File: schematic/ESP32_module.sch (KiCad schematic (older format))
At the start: 14 parts, among them J1 Conn_02x03_Odd_Even, J2 Conn_02x05_Odd_Even, J3 Conn_02x05_Odd_Even, U1 ESP32-WROOM-32

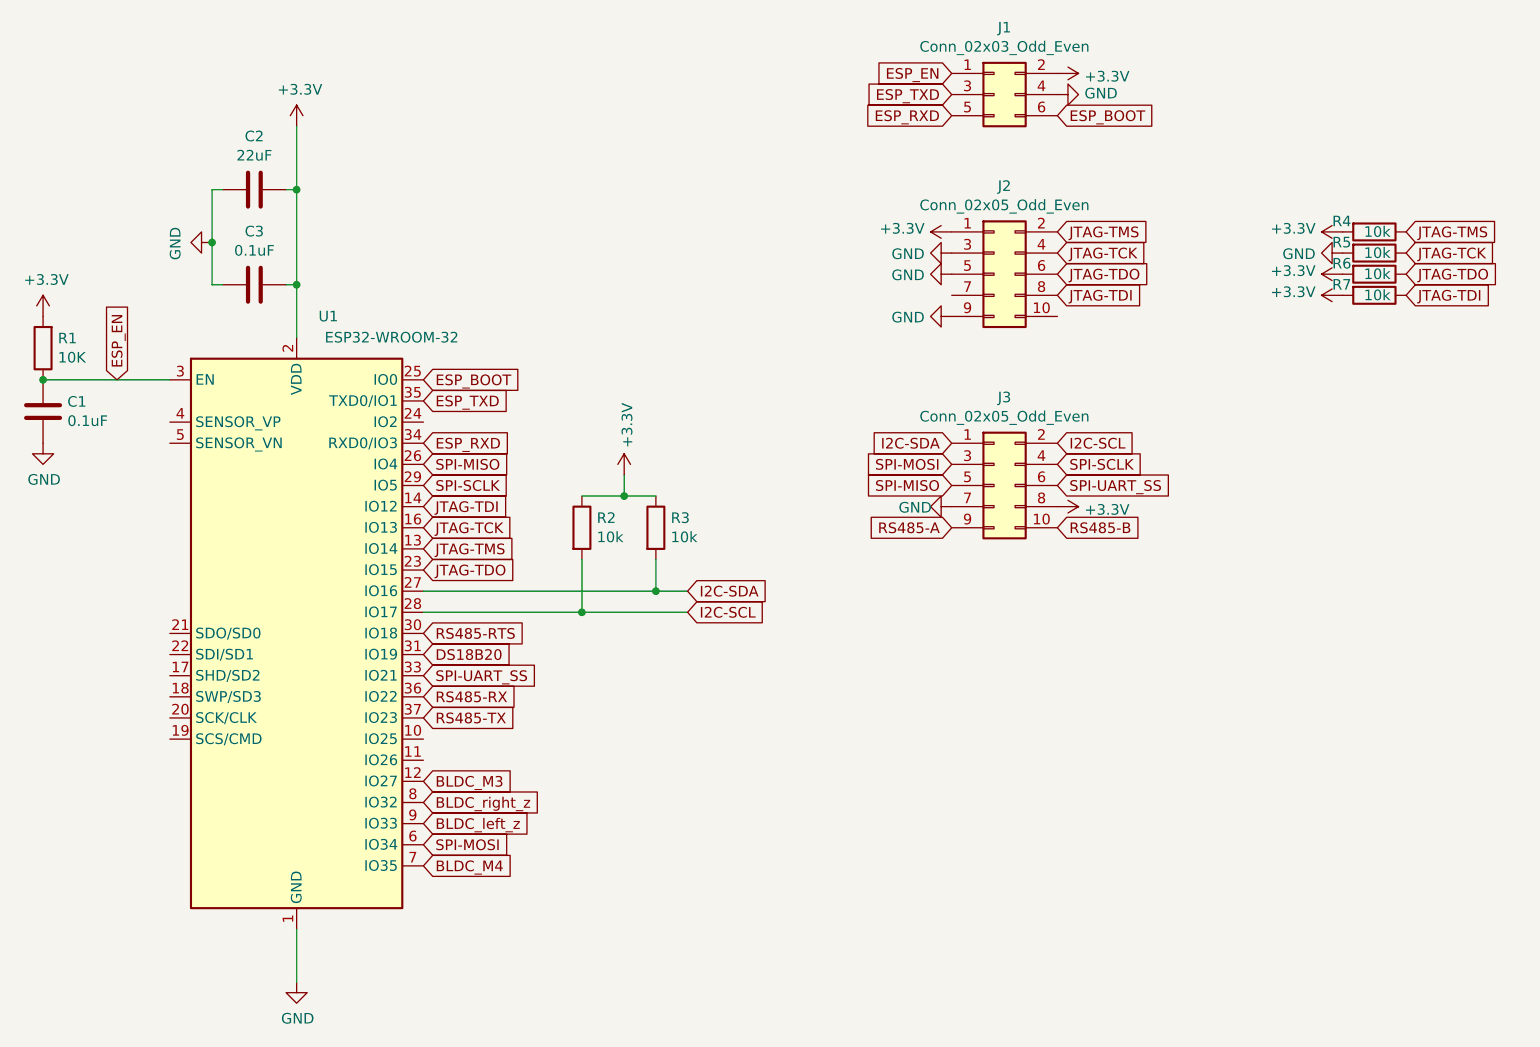
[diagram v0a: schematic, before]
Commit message: SPI SS multiplex concept
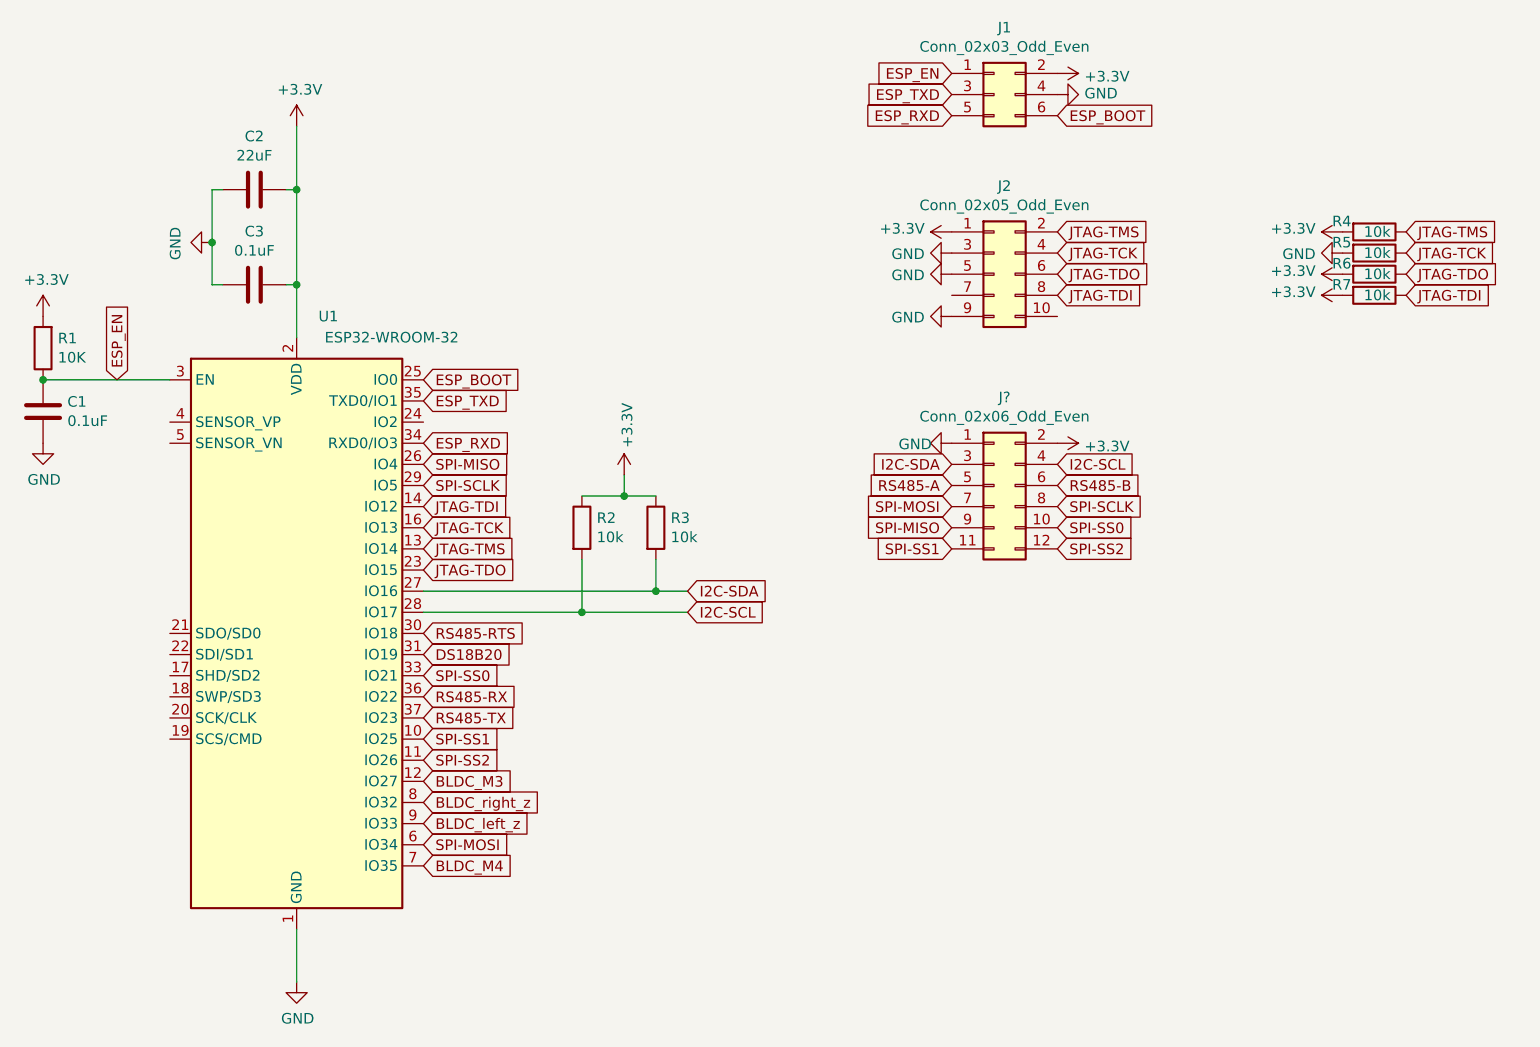
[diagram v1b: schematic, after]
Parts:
- removed J3: Conn_02x05_Odd_Even, Connector_IDC:IDC-Header_2x05_P2.54mm_Vertical, symbol Connector_Generic:Conn_02x05_Odd_Even
- added J?: Conn_02x06_Odd_Even, symbol Connector_Generic:Conn_02x06_Odd_Even
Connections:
- net +3V3: now also J?.2 (Pin_2)
- net GND: now also J?.1 (Pin_1)
- net I2C-SCL: now also J?.4 (Pin_4)
- net I2C-SDA: now also J?.3 (Pin_3)
- net RS485-A: now also J?.5 (Pin_5)
- net RS485-B: now also J?.6 (Pin_6)
- net SPI-MISO: now also J?.9 (Pin_9)
- net SPI-MOSI: now also J?.7 (Pin_7)
- net SPI-SCLK: now also J?.8 (Pin_8)
- net SPI-SS1: now reaches U1.10 (IO25)
- net SPI-SS1: now also J?.11 (Pin_11)
- net SPI-SS2: now reaches U1.11 (IO26)
- net SPI-SS2: now also J?.12 (Pin_12)
- net SPI-UART_SS renamed SPI-SS0
- net SPI-SS0: now also J?.10 (Pin_10)
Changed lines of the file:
@@
 SPI-SCLK
 Text GLabel 3150 4500 2    50   Input ~ 0
-SPI-UART_SS
+SPI-SS0
 Text GLabel 3150 4400 2    50   Input ~ 0
 DS18B20
@@
 	1    0    0    -1
 $EndComp
-$Comp
-L Connector_Generic:Conn_02x05_Odd_Even J?
-U 1 1 5EF14A1B
-P 5850 3600
-AR Path="/5EF14A1B" Ref="J?"  Part="1"
-AR Path="/5ED629AF/5EF14A1B" Ref="J3"  Part="1"
-F 0 "J3" H 5900 4017 50  0000 C CNN
-F 1 "Conn_02x05_Odd_Even" H 5900 3926 50  0000 C CNN
-F 2 "Connector_IDC:IDC-Header_2x05_P2.54mm_Vertical" H 5850 3600 50  0001 C CNN
-F 3 "~" H 5850 3600 50  0001 C CNN
-	1    5850 3600
-	1    0    0    -1
-$EndComp
-Text GLabel 5650 3400 0    50   Input ~ 0
+Text GLabel 5650 3500 0    50   Input ~ 0
 I2C-SDA
-Text GLabel 6150 3400 2    50   Input ~ 0
+Text GLabel 6150 3500 2    50   Input ~ 0
 I2C-SCL
 $Comp
 L power:GND #PWR?
 U 1 1 5EF14A23
-P 5650 3700
+P 5650 3400
 AR Path="/5EF14A23" Ref="#PWR?"  Part="1"
 AR Path="/5ED629AF/5EF14A23" Ref="#PWR011"  Part="1"
-F 0 "#PWR011" H 5650 3450 50  0001 C CNN
-F 1 "GND" V 5655 3527 50  0000 C CNN
-F 2 "" H 5650 3700 50  0001 C CNN
-F 3 "" H 5650 3700 50  0001 C CNN
-	1    5650 3700
+F 0 "#PWR011" H 5650 3150 50  0001 C CNN
+F 1 "GND" V 5655 3227 50  0000 C CNN
+F 2 "" H 5650 3400 50  0001 C CNN
+F 3 "" H 5650 3400 50  0001 C CNN
+	1    5650 3400
 	0    1    1    0
 $EndComp
@@
 L power:+3.3V #PWR?
 U 1 1 5EF14A29
-P 6150 3700
+P 6150 3400
 AR Path="/5EF14A29" Ref="#PWR?"  Part="1"
 AR Path="/5ED629AF/5EF14A29" Ref="#PWR014"  Part="1"
-F 0 "#PWR014" H 6150 3550 50  0001 C CNN
-F 1 "+3.3V" V 6165 3828 50  0000 L CNN
-F 2 "" H 6150 3700 50  0001 C CNN
-F 3 "" H 6150 3700 50  0001 C CNN
-	1    6150 3700
-	0    1    1    0
-$EndComp
+F 0 "#PWR014" H 6150 3250 50  0001 C CNN
+F 1 "+3.3V" V 6165 3528 50  0000 L CNN
+F 2 "" H 6150 3400 50  0001 C CNN
+F 3 "" H 6150 3400 50  0001 C CNN
+	1    6150 3400
+	0    1    1    0
+$EndComp
+Text GLabel 5650 3600 0    50   Input ~ 0
+RS485-A
+Text GLabel 6150 3600 2    50   Input ~ 0
+RS485-B
+Text GLabel 5650 3700 0    50   Input ~ 0
+SPI-MOSI
 Text GLabel 5650 3800 0    50   Input ~ 0
-RS485-A
+SPI-MISO
+Text GLabel 6150 3700 2    50   Input ~ 0
+SPI-SCLK
 Text GLabel 6150 3800 2    50   Input ~ 0
-RS485-B
-Text GLabel 5650 3500 0    50   Input ~ 0
-SPI-MOSI
-Text GLabel 5650 3600 0    50   Input ~ 0
-SPI-MISO
-Text GLabel 6150 3500 2    50   Input ~ 0
-SPI-SCLK
-Text GLabel 6150 3600 2    50   Input ~ 0
-SPI-UART_SS
+SPI-SS0
 $Comp
 L Device:R R1
@@
 	0    1    1    0
 $EndComp
+$Comp
+L Connector_Generic:Conn_02x06_Odd_Even J?
+U 1 1 5EEFB1AB
+P 5850 3600
+F 0 "J?" H 5900 4017 50  0000 C CNN
+F 1 "Conn_02x06_Odd_Even" H 5900 3926 50  0000 C CNN
+F 2 "" H 5850 3600 50  0001 C CNN
+F 3 "~" H 5850 3600 50  0001 C CNN
+	1    5850 3600
+	1    0    0    -1
+$EndComp
+Text GLabel 5650 3900 0    50   Input ~ 0
+SPI-SS1
+Text GLabel 6150 3900 2    50   Input ~ 0
+SPI-SS2
+Text GLabel 3150 4800 2    50   Input ~ 0
+SPI-SS1
+Text GLabel 3150 4900 2    50   Input ~ 0
+SPI-SS2
 $EndSCHEMATC

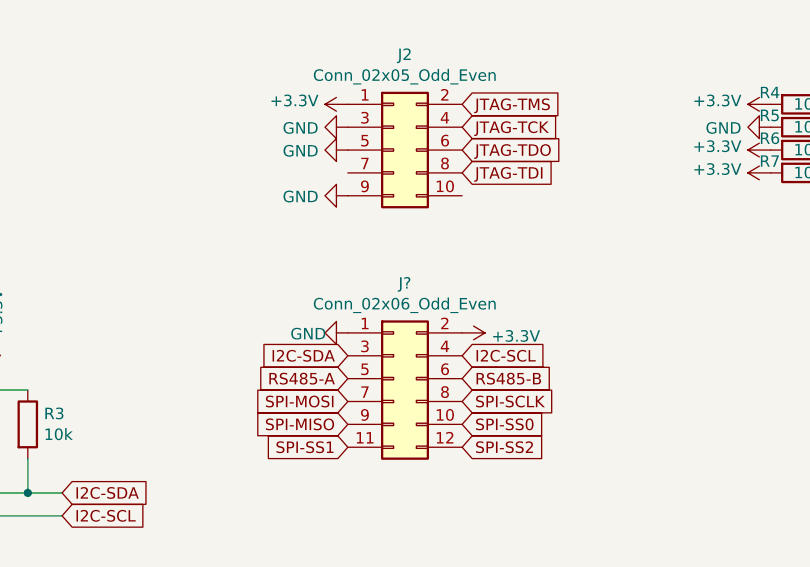
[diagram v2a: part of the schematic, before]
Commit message: added 5v boost converter
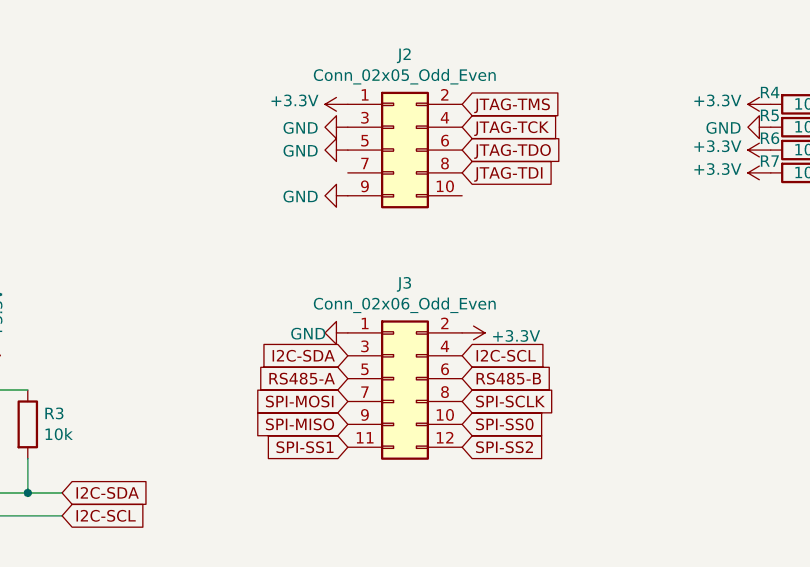
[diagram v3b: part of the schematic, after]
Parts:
- gave numbers to parts that had none: 1
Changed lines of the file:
@@
 $EndComp
 $Comp
-L Connector_Generic:Conn_02x06_Odd_Even J?
+L Connector_Generic:Conn_02x06_Odd_Even J3
 U 1 1 5EEFB1AB
 P 5850 3600
-F 0 "J?" H 5900 4017 50  0000 C CNN
+F 0 "J3" H 5900 4017 50  0000 C CNN
 F 1 "Conn_02x06_Odd_Even" H 5900 3926 50  0000 C CNN
 F 2 "" H 5850 3600 50  0001 C CNN

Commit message: added 14pin header
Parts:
- J3: footprint (none) -> Connector_IDC:IDC-Header_2x06_P2.54mm_Vertical
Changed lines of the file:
@@
 F 0 "J3" H 5900 4017 50  0000 C CNN
 F 1 "Conn_02x06_Odd_Even" H 5900 3926 50  0000 C CNN
-F 2 "" H 5850 3600 50  0001 C CNN
+F 2 "Connector_IDC:IDC-Header_2x06_P2.54mm_Vertical" H 5850 3600 50  0001 C CNN
 F 3 "~" H 5850 3600 50  0001 C CNN
 	1    5850 3600
